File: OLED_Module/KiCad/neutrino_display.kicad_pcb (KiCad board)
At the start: 2 copper layers, 52.5 x 37.5 mm, 7 parts, among them J2 OLED_Headers

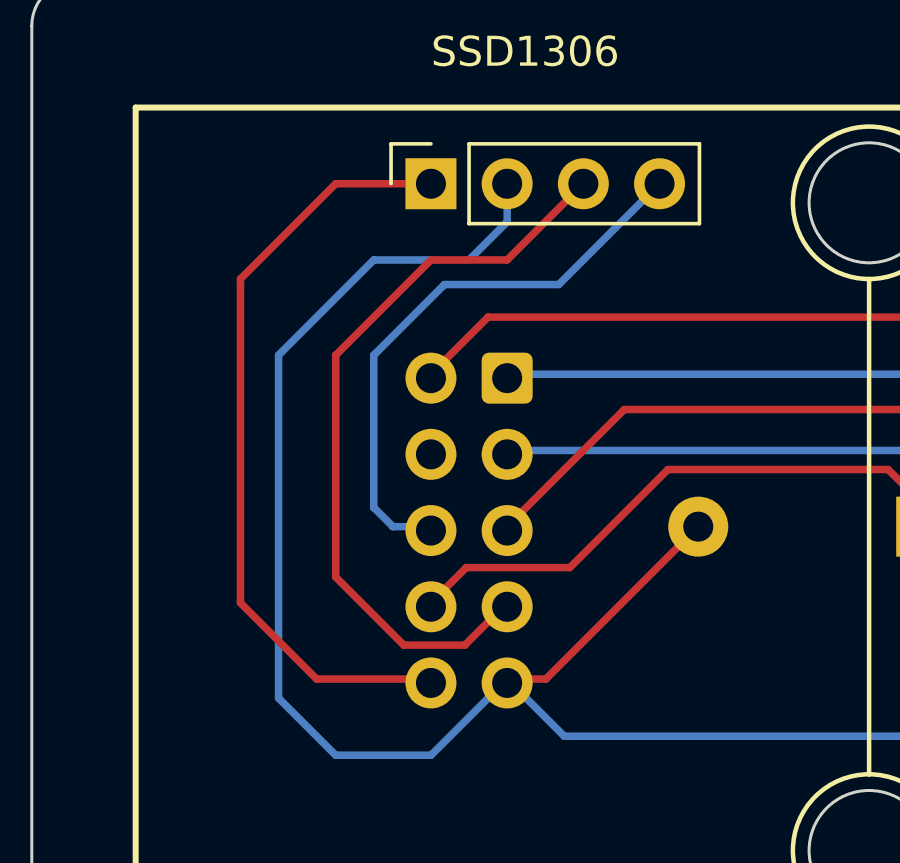
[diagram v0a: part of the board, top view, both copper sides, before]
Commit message: Fixed PCBs, updated firmware, added PrusaSlicer settings, updated README.md, updated BOM. Awesome :)
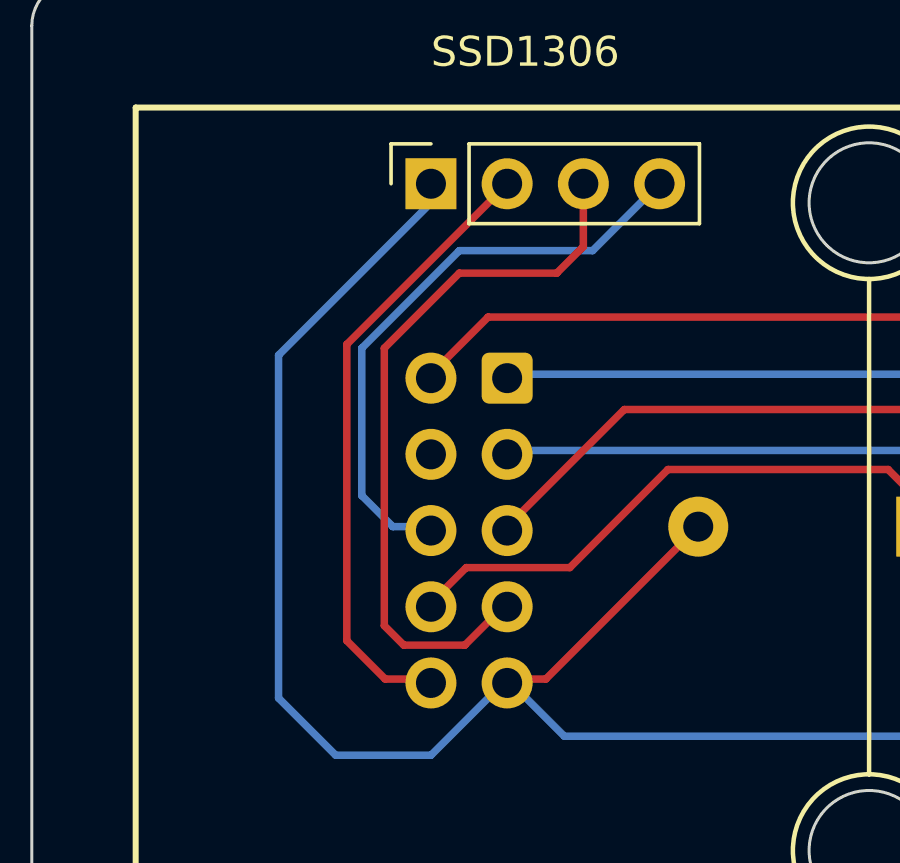
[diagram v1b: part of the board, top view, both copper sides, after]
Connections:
- J2 pad 1: +5V -> GND
- J2 pad 2: GND -> +5V
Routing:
- net +5V: track 25.9 -> 20.8 mm
- net GND: track 102.3 -> 99.3 mm
- net SCL: track 25.3 -> 24.3 mm
- net SDA: track 19.1 -> 19.8 mm
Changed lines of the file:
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@@
       (stroke (width 0.1) (type solid)) (layer "F.Fab"))
     (pad "1" thru_hole rect (at 0 0 90) (size 1.7 1.7) (drill 1) (layers "*.Cu" "*.Mask")
-      (net 10 "+5V") (pinfunction "Pin_1") (pintype "passive"))
+      (net 2 "GND") (pinfunction "Pin_1") (pintype "passive"))
     (pad "2" thru_hole oval (at 0 2.54 90) (size 1.7 1.7) (drill 1) (layers "*.Cu" "*.Mask")
-      (net 2 "GND") (pinfunction "Pin_2") (pintype "passive"))
+      (net 10 "+5V") (pinfunction "Pin_2") (pintype "passive"))
     (pad "3" thru_hole oval (at 0 5.08 90) (size 1.7 1.7) (drill 1) (layers "*.Cu" "*.Mask")
       (net 9 "SCL") (pinfunction "Pin_3") (pintype "passive"))
@@
   (segment (start 160.655 74.93) (end 154.94 80.645) (width 0.25) (layer "F.Cu") (net 2))
   (segment (start 125.095 81.28) (end 126.385 81.28) (width 0.25) (layer "F.Cu") (net 2))
+  (segment (start 122.555 65.405) (end 117.475 70.485) (width 0.25) (layer "B.Cu") (net 2))
   (segment (start 119.38 83.82) (end 122.555 83.82) (width 0.25) (layer "B.Cu") (net 2))
   (segment (start 127 83.185) (end 145.9 83.185) (width 0.25) (layer "B.Cu") (net 2))
-  (segment (start 123.825 67.31) (end 120.65 67.31) (width 0.25) (layer "B.Cu") (net 2))
-  (segment (start 120.65 67.31) (end 117.475 70.485) (width 0.25) (layer "B.Cu") (net 2))
-  (segment (start 122.555 83.82) (end 125.095 81.28) (width 0.25) (layer "B.Cu") (net 2))
   (segment (start 148.44 73.275) (end 148.44 75.565) (width 0.25) (layer "B.Cu") (net 2))
   (segment (start 154.94 80.645) (end 148.44 80.645) (width 0.25) (layer "B.Cu") (net 2))
   (segment (start 117.475 81.915) (end 119.38 83.82) (width 0.25) (layer "B.Cu") (net 2))
-  (segment (start 148.44 75.565) (end 148.44 80.645) (width 0.25) (layer "B.Cu") (net 2))
-  (segment (start 145.9 83.185) (end 148.44 80.645) (width 0.25) (layer "B.Cu") (net 2))
-  (segment (start 125.095 64.77) (end 125.095 66.04) (width 0.25) (layer "B.Cu") (net 2))
   (segment (start 117.475 70.485) (end 117.475 81.915) (width 0.25) (layer "B.Cu") (net 2))
-  (segment (start 125.095 66.04) (end 123.825 67.31) (width 0.25) (layer "B.Cu") (net 2))
+  (segment (start 122.555 64.77) (end 122.555 65.405) (width 0.25) (layer "B.Cu") (net 2))
+  (segment (start 145.9 83.185) (end 148.44 80.645) (width 0.25) (layer "B.Cu") (net 2))
+  (segment (start 148.44 75.565) (end 148.44 80.645) (width 0.25) (layer "B.Cu") (net 2))
   (segment (start 125.095 81.28) (end 127 83.185) (width 0.25) (layer "B.Cu") (net 2))
+  (segment (start 122.555 83.82) (end 125.095 81.28) (width 0.25) (layer "B.Cu") (net 2))
   (segment (start 144.265 69.1) (end 148.44 73.275) (width 0.25) (layer "B.Cu") (net 2))
   (segment (start 142.645 65) (end 152.165 65) (width 0.25) (layer "F.Cu") (net 3))
@@
   (segment (start 129 72.295) (end 125.095 76.2) (width 0.25) (layer "F.Cu") (net 6))
   (segment (start 138.57 72.295) (end 129 72.295) (width 0.25) (layer "F.Cu") (net 6))
-  (segment (start 120.65 75.565) (end 121.285 76.2) (width 0.25) (layer "B.Cu") (net 7))
-  (segment (start 123.005 68.13) (end 120.65 70.485) (width 0.25) (layer "B.Cu") (net 7))
-  (segment (start 126.815 68.13) (end 123.005 68.13) (width 0.25) (layer "B.Cu") (net 7))
-  (segment (start 120.65 70.485) (end 120.65 75.565) (width 0.25) (layer "B.Cu") (net 7))
-  (segment (start 130.175 64.77) (end 126.815 68.13) (width 0.25) (layer "B.Cu") (net 7))
+  (segment (start 123.5 67) (end 120.25 70.25) (width 0.25) (layer "B.Cu") (net 7))
+  (segment (start 120.25 70.25) (end 120.25 75.165) (width 0.25) (layer "B.Cu") (net 7))
+  (segment (start 130.175 64.77) (end 127.945 67) (width 0.25) (layer "B.Cu") (net 7))
   (segment (start 121.285 76.2) (end 122.555 76.2) (width 0.25) (layer "B.Cu") (net 7))
+  (segment (start 127.945 67) (end 123.5 67) (width 0.25) (layer "B.Cu") (net 7))
+  (segment (start 120.25 75.165) (end 121.285 76.2) (width 0.25) (layer "B.Cu") (net 7))
   (segment (start 142.24 78.945) (end 148.44 85.145) (width 0.25) (layer "F.Cu") (net 8))
   (segment (start 142.24 73.025) (end 142.24 78.945) (width 0.25) (layer "F.Cu") (net 8))
@@
   (segment (start 141.3575 72.1425) (end 140.335 71.12) (width 0.25) (layer "B.Cu") (net 8))
   (segment (start 121.65 80.15) (end 123.685 80.15) (width 0.25) (layer "F.Cu") (net 9))
-  (segment (start 119.38 70.485) (end 119.38 77.88) (width 0.25) (layer "F.Cu") (net 9))
-  (segment (start 119.38 77.88) (end 121.65 80.15) (width 0.25) (layer "F.Cu") (net 9))
-  (segment (start 122.555 67.31) (end 119.38 70.485) (width 0.25) (layer "F.Cu") (net 9))
-  (segment (start 127.635 64.77) (end 125.095 67.31) (width 0.25) (layer "F.Cu") (net 9))
-  (segment (start 125.095 67.31) (end 122.555 67.31) (width 0.25) (layer "F.Cu") (net 9))
+  (segment (start 127.635 64.77) (end 127.635 66.865) (width 0.25) (layer "F.Cu") (net 9))
+  (segment (start 127.635 66.865) (end 126.75 67.75) (width 0.25) (layer "F.Cu") (net 9))
+  (segment (start 121 70.25) (end 121 79.5) (width 0.25) (layer "F.Cu") (net 9))
+  (segment (start 126.75 67.75) (end 123.5 67.75) (width 0.25) (layer "F.Cu") (net 9))
   (segment (start 123.685 80.15) (end 125.095 78.74) (width 0.25) (layer "F.Cu") (net 9))
-  (segment (start 122.555 64.77) (end 119.38 64.77) (width 0.25) (layer "F.Cu") (net 10))
-  (segment (start 118.745 81.28) (end 122.555 81.28) (width 0.25) (layer "F.Cu") (net 10))
-  (segment (start 116.205 67.945) (end 116.205 78.74) (width 0.25) (layer "F.Cu") (net 10))
-  (segment (start 119.38 64.77) (end 116.205 67.945) (width 0.25) (layer "F.Cu") (net 10))
-  (segment (start 116.205 78.74) (end 118.745 81.28) (width 0.25) (layer "F.Cu") (net 10))
+  (segment (start 123.5 67.75) (end 121 70.25) (width 0.25) (layer "F.Cu") (net 9))
+  (segment (start 121 79.5) (end 121.65 80.15) (width 0.25) (layer "F.Cu") (net 9))
+  (segment (start 121.03 81.28) (end 122.555 81.28) (width 0.25) (layer "F.Cu") (net 10))
+  (segment (start 119.75 70.125) (end 119.75 80) (width 0.25) (layer "F.Cu") (net 10))
+  (segment (start 125.095 64.77) (end 125.095 64.78) (width 0.25) (layer "F.Cu") (net 10))
+  (segment (start 119.75 80) (end 121.03 81.28) (width 0.25) (layer "F.Cu") (net 10))
+  (segment (start 125.095 64.78) (end 119.75 70.125) (width 0.25) (layer "F.Cu") (net 10))
 )
